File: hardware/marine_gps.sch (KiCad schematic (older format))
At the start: 16 parts, among them CON101 GPIO1, CON102 GPIO3, P101 CONN_02X04, P102 CONN_02X02, P103 CONN_01X04, P104 CONN_01X11, P105 CONN_01X02, P106 CONN_01X06, P107 CONN_01X19, P108 CONN_01X01, P109 CONN_01X05, P110 CONN_01X03, P111 CONN_01X02, P112 CONN_01X05, P113 HE10-10, P114 CONN_01X03

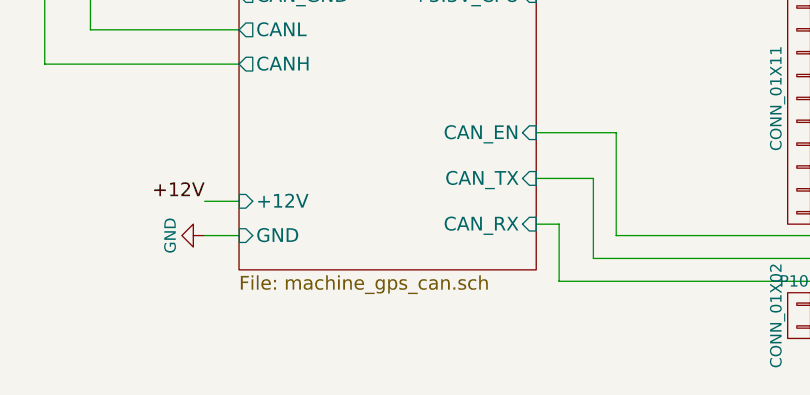
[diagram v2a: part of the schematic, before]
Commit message: Rename machine_gps_can to marine_gps_can (typo)
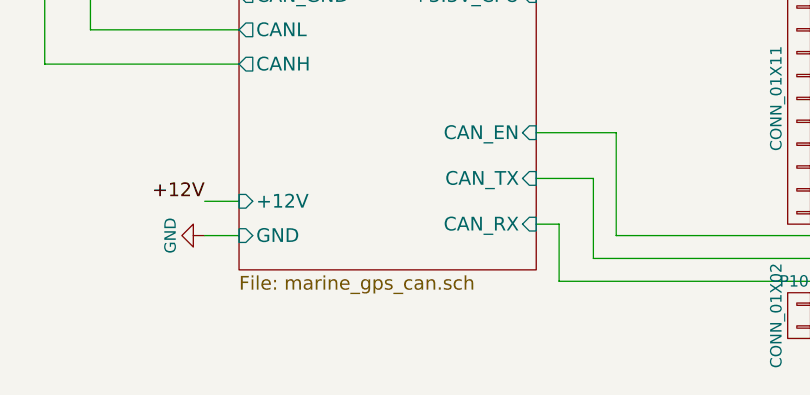
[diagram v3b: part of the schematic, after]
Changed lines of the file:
@@
 U 56A7D2C0
 F0 "Marine GPS CAN" 60
-F1 "machine_gps_can.sch" 60
+F1 "marine_gps_can.sch" 60
 F2 "CAN_RX" I R 3050 5300 60
 F3 "CAN_TX" I R 3050 5100 60
@@
 $Comp
 L FL40YA-V36P-2X20-LF CON101
-U 1 1 56EDEDC1
+U 1 1 00000000
 P 5150 2450
 F 0 "CON101" H 4950 3480 50  0000 L BNN
@@
 $Comp
 L FL40YA-V36P-2X20-LF CON102
-U 1 1 56EDEDC2
+U 1 1 00000000
 P 5150 4850
 F 0 "CON102" H 4950 5880 50  0000 L BNN
@@
 $Comp
 L GNDD #PWR102
-U 1 1 56EDEDC3
+U 1 1 00000000
 P 5400 1200
 F 0 "#PWR102" H 5400 950 50  0001 C CNN
@@
 $Comp
 L CONN_01X02 P111
-U 1 1 56EDEDC4
+U 1 1 00000000
 P 7600 3400
 F 0 "P111" H 7750 3400 50  0000 C CNN
@@
 $Comp
 L CONN_01X05 P109
-U 1 1 56EDEDC5
+U 1 1 00000000
 P 6300 3050
 F 0 "P109" H 6300 3400 50  0000 C CNN
@@
 $Comp
 L CONN_01X03 P110
-U 1 1 56EDEDC6
+U 1 1 00000000
 P 6850 2650
 F 0 "P110" H 6850 2850 50  0000 C CNN
@@
 $Comp
 L GNDD #PWR103
-U 1 1 56EDEDC7
+U 1 1 00000000
 P 6550 2550
 F 0 "#PWR103" H 6550 2300 50  0001 C CNN
@@
 $Comp
 L CONN_01X06 P106
-U 1 1 56EDEDC8
+U 1 1 00000000
 P 4250 1900
 F 0 "P106" H 4250 2200 50  0000 C CNN
@@
 $Comp
 L CONN_01X04 P103
-U 1 1 56EDEDC9
+U 1 1 00000000
 P 4150 3200
 F 0 "P103" H 4150 3450 50  0000 C CNN
@@
 $Comp
 L CONN_02X04 P101
-U 1 1 56EDEDC0
+U 1 1 00000000
 P 3700 3900
 F 0 "P101" H 3700 4150 50  0000 C CNN
@@
 $Comp
 L GND #PWR101
-U 1 1 56EDEDCB
+U 1 1 00000000
 P 1600 5350
 F 0 "#PWR101" H 1600 5100 50  0001 C CNN
@@
 $Comp
 L CONN_01X19 P107
-U 1 1 56EDEDCC
+U 1 1 00000000
 P 6150 4850
 F 0 "P107" H 6150 5850 50  0000 C CNN
@@
 $Comp
 L CONN_01X02 P105
-U 1 1 56EDEDCD
+U 1 1 00000000
 P 4200 5700
 F 0 "P105" H 4200 5850 50  0000 C CNN
@@
 $Comp
 L CONN_01X11 P104
-U 1 1 56EDEDCE
+U 1 1 00000000
 P 4200 4750
 F 0 "P104" H 4200 5300 50  0000 C CNN
@@
 $Comp
 L PWR_FLAG #FLG106
-U 1 1 56EDEDCF
+U 1 1 00000000
 P 5600 1050
 F 0 "#FLG106" H 5600 1145 50  0001 C CNN
@@
 $Comp
 L PWR_FLAG #FLG105
-U 1 1 56EDEDD0
+U 1 1 00000000
 P 4750 1300
 F 0 "#FLG105" H 4750 1395 50  0001 C CNN
@@
 $Comp
 L PWR_FLAG #FLG104
-U 1 1 56EDEDD1
+U 1 1 00000000
 P 4400 1300
 F 0 "#FLG104" H 4400 1395 50  0001 C CNN
@@
 $Comp
 L PWR_FLAG #FLG107
-U 1 1 56EDEDD2
+U 1 1 00000000
 P 5950 1200
 F 0 "#FLG107" H 5950 1295 50  0001 C CNN
@@
 $Comp
 L PWR_FLAG #FLG101
-U 1 1 56EDEDD3
+U 1 1 00000000
 P 3150 3250
 F 0 "#FLG101" H 3150 3345 50  0001 C CNN
@@
 $Comp
 L PWR_FLAG #FLG102
-U 1 1 56EDEDB6
+U 1 1 00000000
 P 3250 3450
 F 0 "#FLG102" H 3250 3545 50  0001 C CNN
@@
 $Comp
 L PWR_FLAG #FLG103
-U 1 1 56EDEDAD
+U 1 1 00000000
 P 3350 3650
 F 0 "#FLG103" H 3350 3745 50  0001 C CNN
@@
 $Comp
 L CONN_01X05 P112
-U 1 1 56EDEDAE
+U 1 1 00000000
 P 6800 2050
 F 0 "P112" H 6800 2250 50  0000 C CNN
@@
 $Comp
 L HE10-10 P113
-U 1 1 56EDEDAF
+U 1 1 00000000
 P 1100 3400
 F 0 "P113" H 1100 3950 50  0000 C CNN
@@
 $Comp
 L CONN_02X02 P102
-U 1 1 56EDEDB0
+U 1 1 00000000
 P 6600 1500
 F 0 "P102" H 6600 1650 50  0000 C CNN
@@
 $Comp
 L CONN_01X03 P114
-U 1 1 56EDEDB1
+U 1 1 00000000
 P 7000 1050
 F 0 "P114" H 7000 1250 50  0000 C CNN
@@
 $Comp
 L CONN_01X01 P108
-U 1 1 56EDEDB2
+U 1 1 00000000
 P 6300 1700
 F 0 "P108" H 6300 1800 50  0000 C CNN
